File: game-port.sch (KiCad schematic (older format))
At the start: 18 parts, among them IC1 74LS244, IC2 NE558, IC6 74LS32, J1 GAME PORT

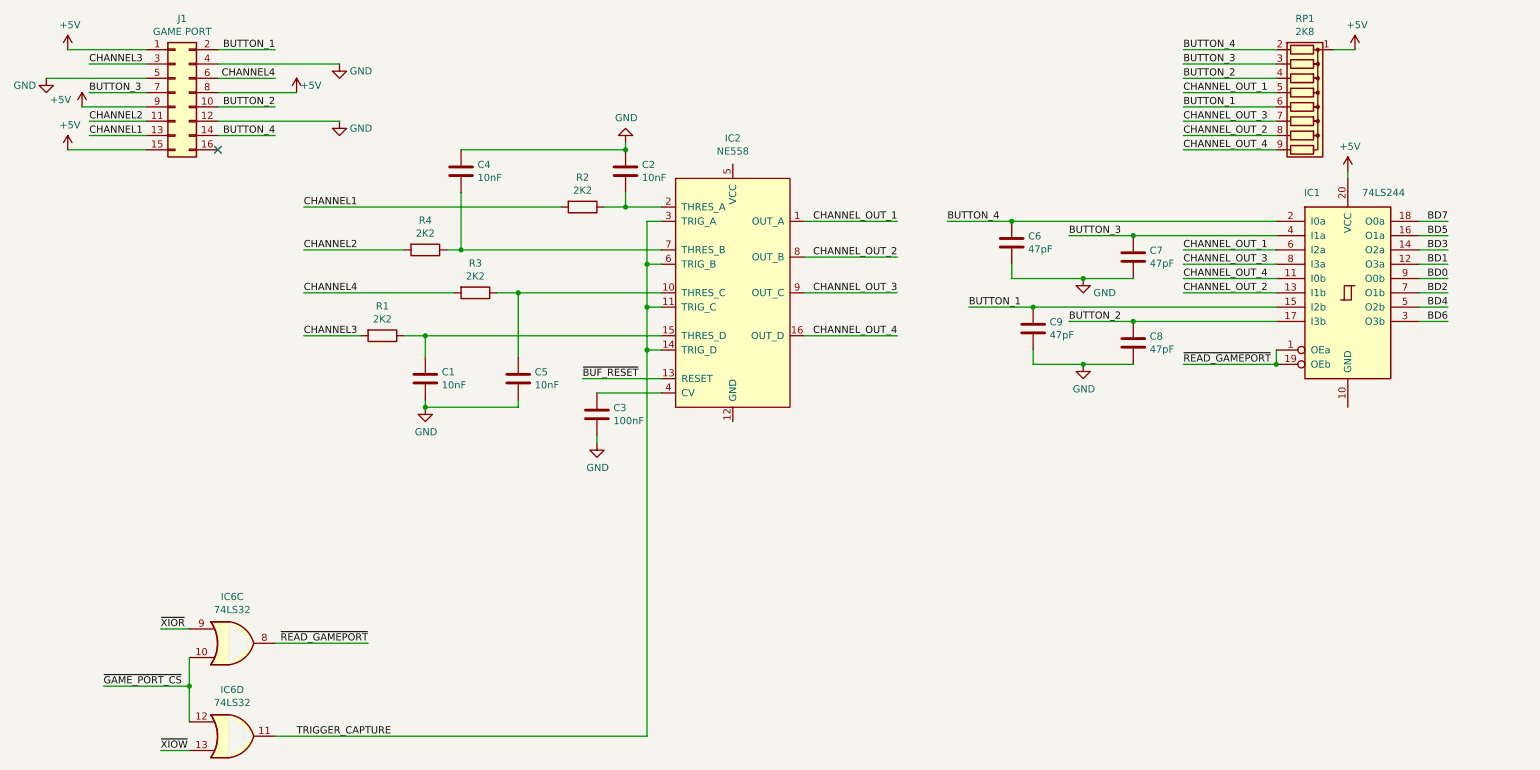
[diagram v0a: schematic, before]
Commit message: Tidy up and map all signals
This fixes up the schematic to:
 - Look presentable
 - Fix all labels connecting sheets
 - Tidy up all loose ends by either inspecting the PCB under
    magnification, measuring with an oscillosope or buzzing
    out with a meter
 - Pass ERC (with 1 exception due to incorrect circuitry around
    pin 33 on the FPU (~RQ~/~GT1~)
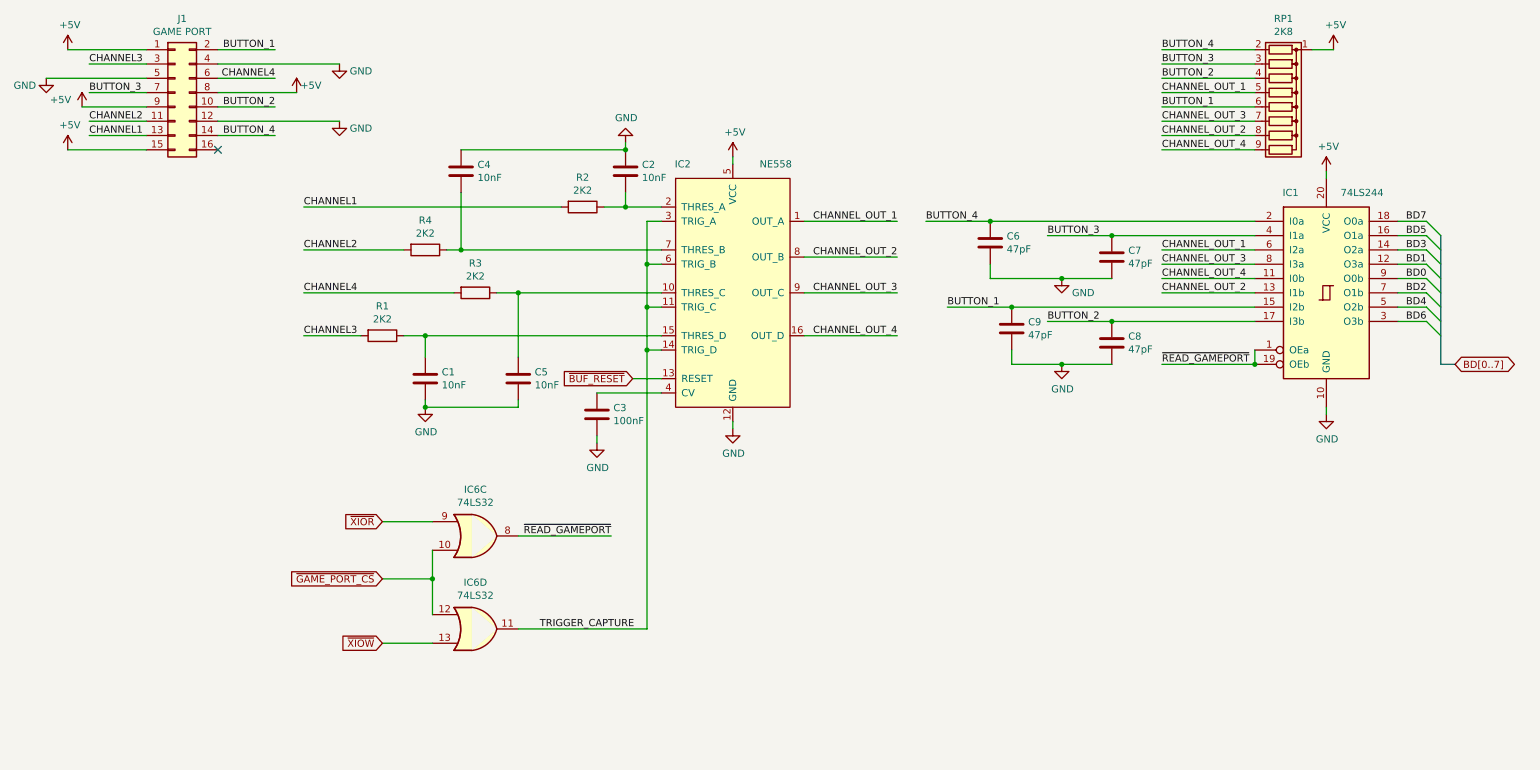
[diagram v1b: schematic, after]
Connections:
- net +5V: now also IC2.5 (VCC)
- net GND: now also IC1.10 (GND), IC2.12 (GND)
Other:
- moved on the sheet: C6, C7, C8, C9, IC1, IC6C, IC6D, RP1
